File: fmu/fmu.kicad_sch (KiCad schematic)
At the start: 0 parts

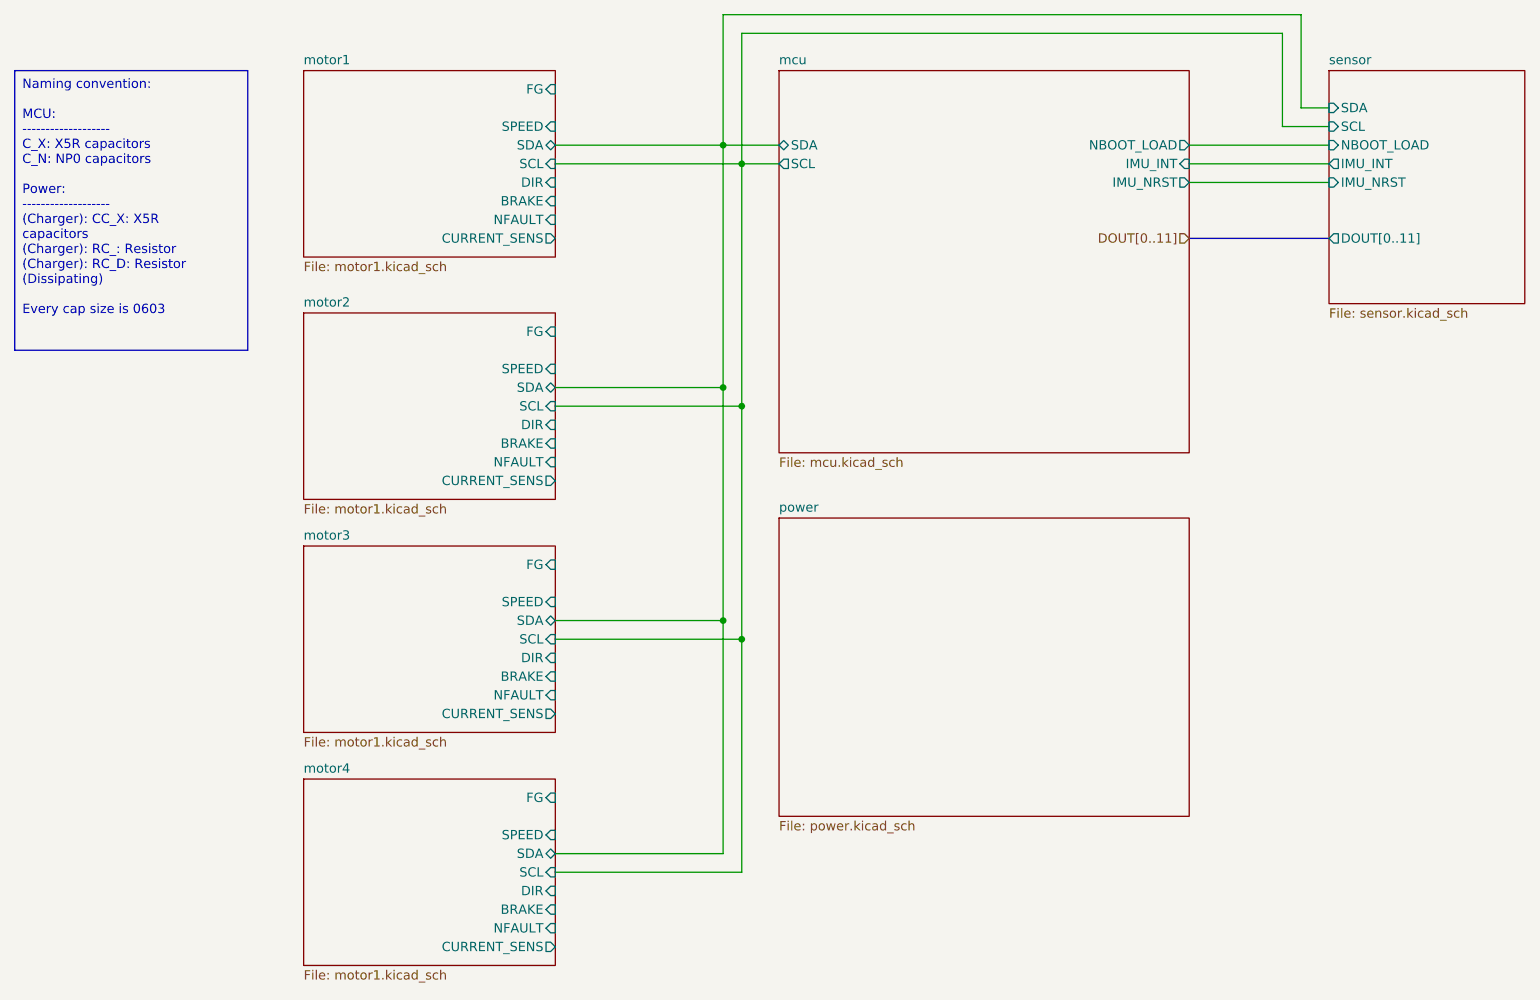
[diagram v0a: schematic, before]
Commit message: Connect motors and MCU
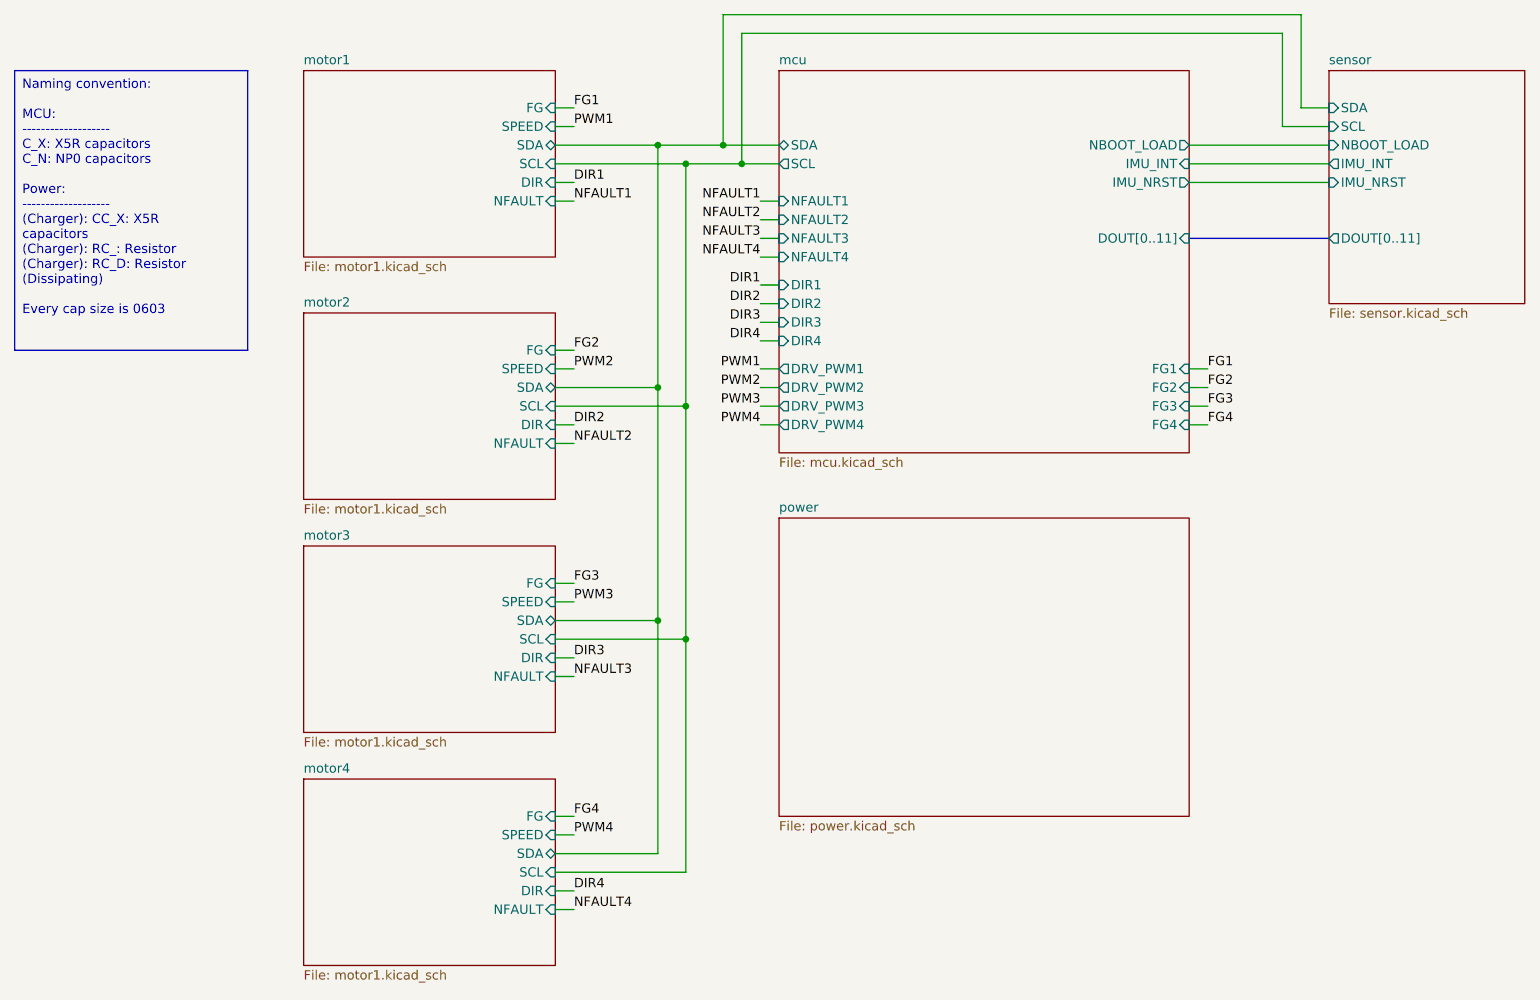
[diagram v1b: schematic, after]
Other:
- sheet mcu ports: added DIR1, DIR2, DIR3, DIR4, DOUT[0..11], DRV_PWM1, DRV_PWM2, DRV_PWM3, DRV_PWM4, FG1, FG2, FG3, FG4, NFAULT1, NFAULT2, NFAULT3, NFAULT4; removed none
- sheet motor1 ports: added none; removed BRAKE, CURRENT_SENS
- sheet motor2 ports: added none; removed BRAKE, CURRENT_SENS
- sheet motor3 ports: added none; removed BRAKE, CURRENT_SENS
- sheet motor4 ports: added none; removed BRAKE, CURRENT_SENS

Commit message: Add voltage regulators
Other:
- sheet sensor ports: added CAM_OFF, FRAME_VALID, LINE_VALID, PIXCLK; removed none
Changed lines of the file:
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@@
+			)
+		)
+		(pin "FRAME_VALID" output
+			(at 198.12 63.5 180)
+			(effects
+				(font
+					(size 1.27 1.27)
+				)
+				(justify left)
+			)
+		)
+		(pin "LINE_VALID" output
+			(at 198.12 66.04 180)
+			(effects
+				(font
+					(size 1.27 1.27)
+				)
+				(justify left)
+			)
+		)
+		(pin "PIXCLK" output
+			(at 198.12 68.58 180)
+			(effects
+				(font
+					(size 1.27 1.27)
+				)
+				(justify left)
+			)
+		)
+		(pin "CAM_OFF" input
+			(at 198.12 57.15 180)
+			(effects
+				(font
+					(size 1.27 1.27)
+				)
+				(justify left)
 			)
 		)

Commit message: Fix some connections
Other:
- sheet mcu ports: added FRAME_VALID, LINE_VALID, PIXCLK; removed none
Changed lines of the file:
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@@
+	(wire
+		(pts
+			(xy 179.07 63.5) (xy 198.12 63.5)
+		)
+		(stroke
+			(width 0)
+			(type default)
+		)
+	)
 	(wire
 		(pts
@@
 	(wire
 		(pts
+			(xy 179.07 68.58) (xy 198.12 68.58)
+		)
+		(stroke
+			(width 0)
+			(type default)
+		)
+	)
+	(wire
+		(pts
 			(xy 106.68 48.26) (xy 106.68 81.28)
 		)
@@
 		(pts
 			(xy 92.71 48.26) (xy 106.68 48.26)
+		)
+		(stroke
+			(width 0)
+			(type default)
+		)
+	)
+	(wire
+		(pts
+			(xy 179.07 66.04) (xy 198.12 66.04)
 		)
 		(stroke
@@
 			(effects
 				(font
+					(size 1.27 1.27)
+				)
+				(justify right)
+			)
+		)
+		(pin "PIXCLK" input
+			(at 179.07 68.58 0)
+			(effects
+				(font
+					(size 1.27 1.27)
+				)
+				(justify right)
+			)
+		)
+		(pin "LINE_VALID" input
+			(at 179.07 66.04 0)
+			(effects
+				(font
+					(size 1.27 1.27)
+				)
+				(justify right)
+			)
+		)
+		(pin "FRAME_VALID" input
+			(at 179.07 63.5 0)
+			(effects
+				(font
